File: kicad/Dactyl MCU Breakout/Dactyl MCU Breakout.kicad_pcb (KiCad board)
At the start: 4 copper layers, 99 x 61.1 mm, 74 parts, among them J202 Split, J203 Column, J204 Thumb, J205 External, J206 Row, J207 Display, J208 Vic, J209 JST, J302 Split, J303 Column, J304 Thumb, J305 External, J306 Row, J307 Display, J308 Vic, J309 JST, SW201 Battery, SW202 Reset, SW203 LED, SW301 Battery, SW302 Reset, SW303 LED, U201 SRV05-4, U202 Nice!Nano/2040, U301 SRV05-4, U302 Nice!Nano/2040

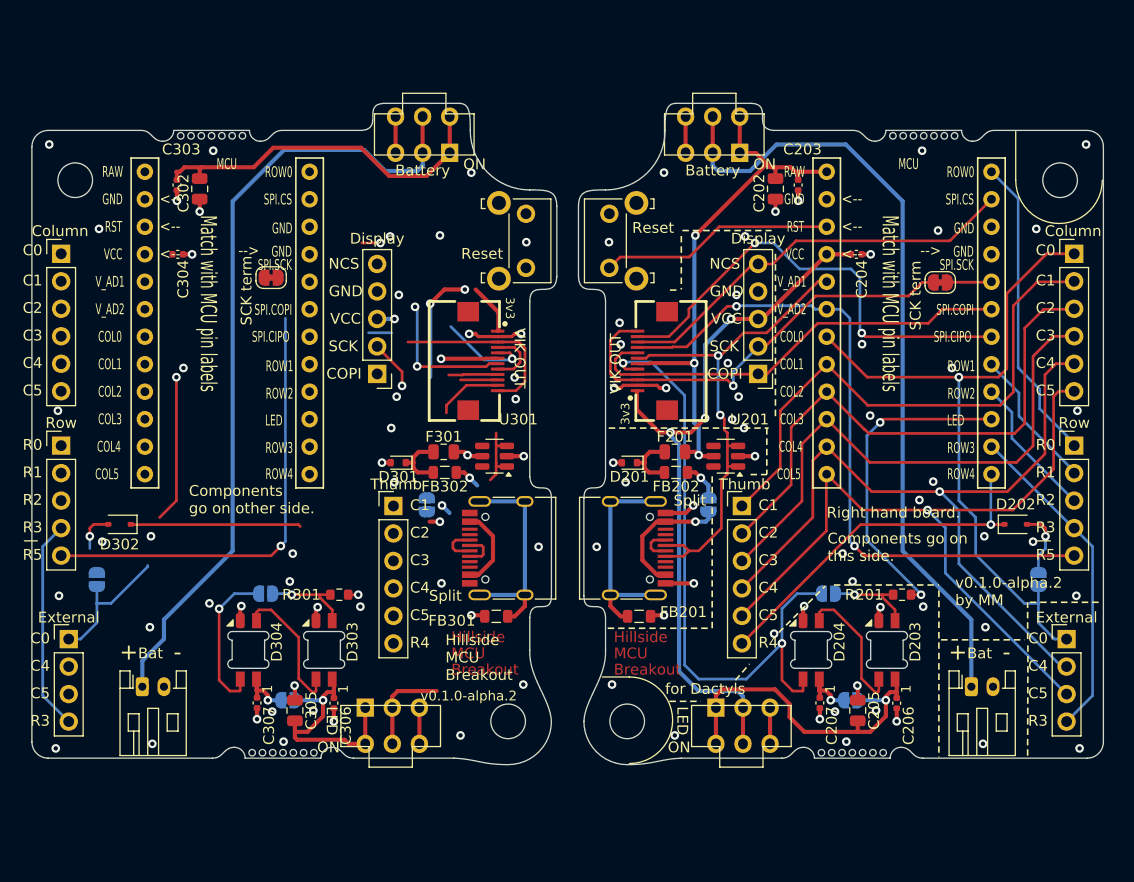
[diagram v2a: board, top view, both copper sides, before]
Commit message: feat(scheme): fix some mislabels
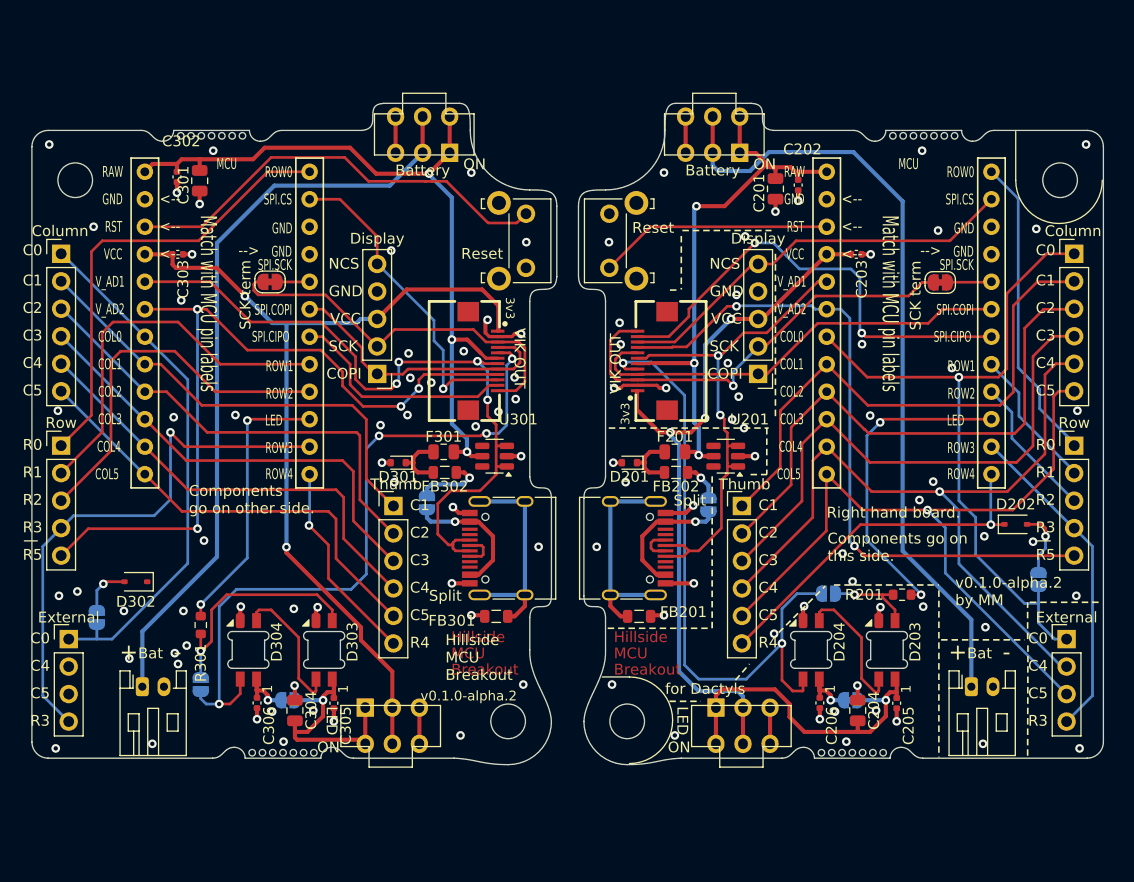
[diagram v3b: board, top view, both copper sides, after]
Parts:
- moved R301 13.1 mm to (65.6, 95.7), turned to -90 degrees
- moved JP304 10.3 mm to (65.6, 101.2), turned to -90 degrees
- moved D302 5.51 mm to (59.6, 91.7)
- moved JP302 3.50 mm to (56.0, 95.0)
- moved C301 0.75 mm to (65.5, 54.6)
- moved C302 0.75 mm to (63.4, 54.3)
- moved JP303 0.41 mm to (72.0, 64.0)
- moved JP301 0.20 mm to (86.5, 84.4)
- renumbered C202 to C201, C203 to C202, C204 to C203, C205 to C204, C206 to C205, C207 to C206, C302 to C301, C303 to C302, C304 to C303, C305 to C304, C306 to C305, C307 to C306, J209 to J201, J309 to J301
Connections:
- C301 pad 2: /Right/RAW -> /Left/RAW
- C302 pad 2: /Right/RAW -> /Left/RAW
- C303 pad 2: /Right/VCC -> /Left/VCC
- C304 pad 2: /Right/VCC_LED1 -> /Left/VCC_LED1
- C305 pad 2: /Right/VCC_LED1 -> /Left/VCC_LED1
- C306 pad 2: /Right/VCC_LED2 -> /Left/VCC_LED2
- D301 pad 1: /Right/RAW_BEADED -> /Left/RAW_BEADED
- D302 pad 1: /Right/row4 -> /Left/row4
- D302 pad 2: Net-(D202-A) -> Net-(D302-A)
- D303 pad 1: /Right/VCC_LED1 -> /Left/VCC_LED1
- D303 pad 2: Net-(D203-DOUT) -> Net-(D303-DOUT)
- D303 pad 4: Net-(D203-DIN) -> Net-(D303-DIN)
- D304 pad 1: /Right/VCC_LED2 -> /Left/VCC_LED2
- D304 pad 2: /Right/LED_out -> /Left/LED_out
- D304 pad 4: Net-(D203-DOUT) -> Net-(D303-DOUT)
- F301 pad 1: /Right/RAW_BEADED -> /Left/RAW_BEADED
- F301 pad 2: /Right/RAW -> /Left/RAW
- FB301 pad 1: /Right/SHIELD -> /Left/SHIELD
- FB302 pad 1: /Right/RAW_ENABLED -> /Left/RAW_ENABLED
- FB302 pad 2: /Right/RAW_BEADED -> /Left/RAW_BEADED
- J301 pad 1: /Right/bat+ -> /Left/bat+
- J302 pad A4: /Right/split_RAW -> /Left/split_RAW
- J302 pad A5: unconnected-(J202-CC1-PadA5) -> unconnected-(J302-CC1-PadA5)
- J302 pad A6: /Right/SPLIT_VIK_GP_AD1 -> /Left/SPLIT_VIK_GP_AD1
- J302 pad A7: Net-(J202-D--PadA7) -> Net-(J302-D--PadA7)
- J302 pad A8: unconnected-(J202-SBU1-PadA8) -> unconnected-(J302-SBU1-PadA8)
- J302 pad A9: /Right/split_RAW -> /Left/split_RAW
- J302 pad B4: /Right/split_RAW -> /Left/split_RAW
- J302 pad B5: unconnected-(J202-CC2-PadB5) -> unconnected-(J302-CC2-PadB5)
- J302 pad B6: /Right/SPLIT_VIK_GP_AD1 -> /Left/SPLIT_VIK_GP_AD1
- J302 pad B7: Net-(J202-D--PadA7) -> Net-(J302-D--PadA7)
- J302 pad B8: unconnected-(J202-SBU2-PadB8) -> unconnected-(J302-SBU2-PadB8)
- J302 pad B9: /Right/split_RAW -> /Left/split_RAW
- J302 pad S1: /Right/SHIELD -> /Left/SHIELD
- J303 pad 1: /Right/col0 -> /Left/col0
- J303 pad 2: /Right/col1 -> /Left/col1
- J303 pad 3: /Right/col2 -> /Left/col2
- J303 pad 4: /Right/col3 -> /Left/col3
- J303 pad 5: /Right/col4 -> /Left/col4
- J303 pad 6: /Right/col5 -> /Left/col5
- J304 pad 1: /Right/col1 -> /Left/col1
- J304 pad 2: /Right/col2 -> /Left/col2
- J304 pad 3: /Right/col3 -> /Left/col3
- J304 pad 4: /Right/col4 -> /Left/col4
- J304 pad 5: /Right/col5 -> /Left/col5
- J304 pad 6: /Right/row4 -> /Left/row4
- J305 pad 1: /Right/col0 -> /Left/col0
- J305 pad 2: /Right/col4 -> /Left/col4
- J305 pad 3: /Right/col5 -> /Left/col5
- J305 pad 4: /Right/row3 -> /Left/row3
- J306 pad 1: /Right/row0 -> /Left/row0
- J306 pad 2: /Right/row1 -> /Left/row1
- J306 pad 3: /Right/row2 -> /Left/row2
- J306 pad 4: /Right/row3 -> /Left/row3
- J306 pad 5: /Right/row5_VIK_GP_AD2 -> /Left/row5_VIK_GP_AD2
- J307 pad 1: /Right/SPI0.COPI/SCL -> /Left/SPI0.COPI/SCL
- J307 pad 2: /Right/SPI0.SCK/SDA -> /Left/SPI0.SCK/SDA
- J307 pad 3: /Right/VCC -> /Left/VCC
- J307 pad 5: /Right/SPI0.SC -> /Left/SPI0.SC
- J308 pad 1: /Right/VCC -> /Left/VCC
- J308 pad 10: /Right/SPI0.SC -> /Left/SPI0.SC
- J308 pad 11: /Right/SPI0.CIPO -> /Left/SPI0.CIPO
- J308 pad 12: /Right/SPI0.SCK/SDA -> /Left/SPI0.SCK/SDA
- J308 pad 3: /Right/SPI0.SCK/SDA -> /Left/SPI0.SCK/SDA
- J308 pad 4: /Right/SPI0.COPI/SCL -> /Left/SPI0.COPI/SCL
- J308 pad 5: /Right/LED_out -> /Left/LED_out
- J308 pad 6: /Right/RAW -> /Left/RAW
- J308 pad 7: /Right/SPLIT_VIK_GP_AD1 -> /Left/SPLIT_VIK_GP_AD1
- J308 pad 8: /Right/SPI0.COPI/SCL -> /Left/SPI0.COPI/SCL
- J308 pad 9: /Right/row5_VIK_GP_AD2 -> /Left/row5_VIK_GP_AD2
- JP301 pad 1: /Right/split_RAW -> /Left/split_RAW
- JP301 pad 2: /Right/RAW_ENABLED -> /Left/RAW_ENABLED
- JP302 pad 1: /Right/col0 -> /Left/col0
- JP302 pad 2: Net-(D202-A) -> Net-(D302-A)
- JP303 pad 1: Net-(JP203-A) -> Net-(JP303-A)
- JP303 pad 2: /Right/SPI0.SCK/SDA -> /Left/SPI0.SCK/SDA
- JP304 pad 1: Net-(D203-DIN) -> Net-(D303-DIN)
- JP304 pad 2: /Right/LED_out -> /Left/LED_out
- JP305 pad 1: /Right/VCC_LED1 -> /Left/VCC_LED1
- JP305 pad 2: /Right/VCC_LED2 -> /Left/VCC_LED2
- R301 pad 1: /Right/LED -> /Left/LED
- R301 pad 2: Net-(D203-DIN) -> Net-(D303-DIN)
- SW301 pad 1: /Right/RAW -> /Left/RAW
- SW301 pad 2: /Right/bat+ -> /Left/bat+
- SW301 pad 3: unconnected-(SW201-C-Pad3)_0 -> unconnected-(SW301-C-Pad3)_0
- SW302 pad 2: /Right/RST -> /Left/RST
- SW303 pad 1: /Right/VCC_LED1 -> /Left/VCC_LED1
- SW303 pad 2: /Right/VCC -> /Left/VCC
- SW303 pad 3: unconnected-(SW203-C-Pad3)_0 -> unconnected-(SW303-C-Pad3)_1
- U301 pad 1: /Right/SPLIT_VIK_GP_AD1 -> /Left/SPLIT_VIK_GP_AD1
- U301 pad 3: /Right/SPLIT_VIK_GP_AD1 -> /Left/SPLIT_VIK_GP_AD1
- U301 pad 4: unconnected-(U201-IO3-Pad4) -> unconnected-(U301-IO3-Pad4)
- U301 pad 5: /Right/RAW -> /Left/RAW
- U301 pad 6: unconnected-(U201-IO4-Pad6) -> unconnected-(U301-IO4-Pad6)
- U302 pad 1: /Right/row0 -> /Left/row0
- U302 pad 10: /Right/LED -> /Left/LED
- U302 pad 11: /Right/row3 -> /Left/row3
- U302 pad 12: /Right/row4 -> /Left/row4
- U302 pad 13: /Right/col5 -> /Left/col5
- U302 pad 14: /Right/col4 -> /Left/col4
- U302 pad 15: /Right/col3 -> /Left/col3
- U302 pad 16: /Right/col2 -> /Left/col2
- U302 pad 17: /Right/col1 -> /Left/col1
- U302 pad 18: /Right/col0 -> /Left/col0
- U302 pad 19: /Right/row5_VIK_GP_AD2 -> /Left/row5_VIK_GP_AD2
- U302 pad 2: /Right/SPI0.SC -> /Left/SPI0.SC
- U302 pad 20: /Right/SPLIT_VIK_GP_AD1 -> /Left/SPLIT_VIK_GP_AD1
- U302 pad 21: /Right/VCC -> /Left/VCC
- U302 pad 22: /Right/RST -> /Left/RST
- U302 pad 24: /Right/RAW -> /Left/RAW
- U302 pad 5: Net-(JP203-A) -> Net-(JP303-A)
- U302 pad 6: /Right/SPI0.COPI/SCL -> /Left/SPI0.COPI/SCL
- U302 pad 7: /Right/SPI0.CIPO -> /Left/SPI0.CIPO
- U302 pad 8: /Right/row1 -> /Left/row1
- U302 pad 9: /Right/row2 -> /Left/row2
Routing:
- net /Left/VCC: track 0.00 -> 79.7 mm, vias 0 -> 2
- net /Left/row5_VIK_GP_AD2: track 0.00 -> 72.7 mm, vias 0 -> 4
- net /Right/bat+: track 139.6 -> 69.0 mm
- net /Left/SPLIT_VIK_GP_AD1: track 0.00 -> 68.2 mm, vias 0 -> 4
- net /Left/RAW: track 0.00 -> 67.5 mm, vias 0 -> 3
- net /Left/bat+: track 0.00 -> 66.3 mm
- net /Left/LED_out: track 0.00 -> 63.8 mm, vias 0 -> 4
- net /Left/row3: track 0.00 -> 50.4 mm, vias 0 -> 1
- net /Left/col0: track 0.00 -> 48.7 mm
- net /Right/row5_VIK_GP_AD2: track 110.1 -> 63.6 mm, vias 3 -> 2
- net /Left/col2: track 0.00 -> 42.8 mm
- net /Left/col1: track 0.00 -> 42.5 mm
- net /Left/row0: track 0.00 -> 42.3 mm
- net /Left/col3: track 0.00 -> 42.0 mm
- net /Left/col4: track 0.00 -> 41.6 mm
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
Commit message: feat(pcb): finish routing left board
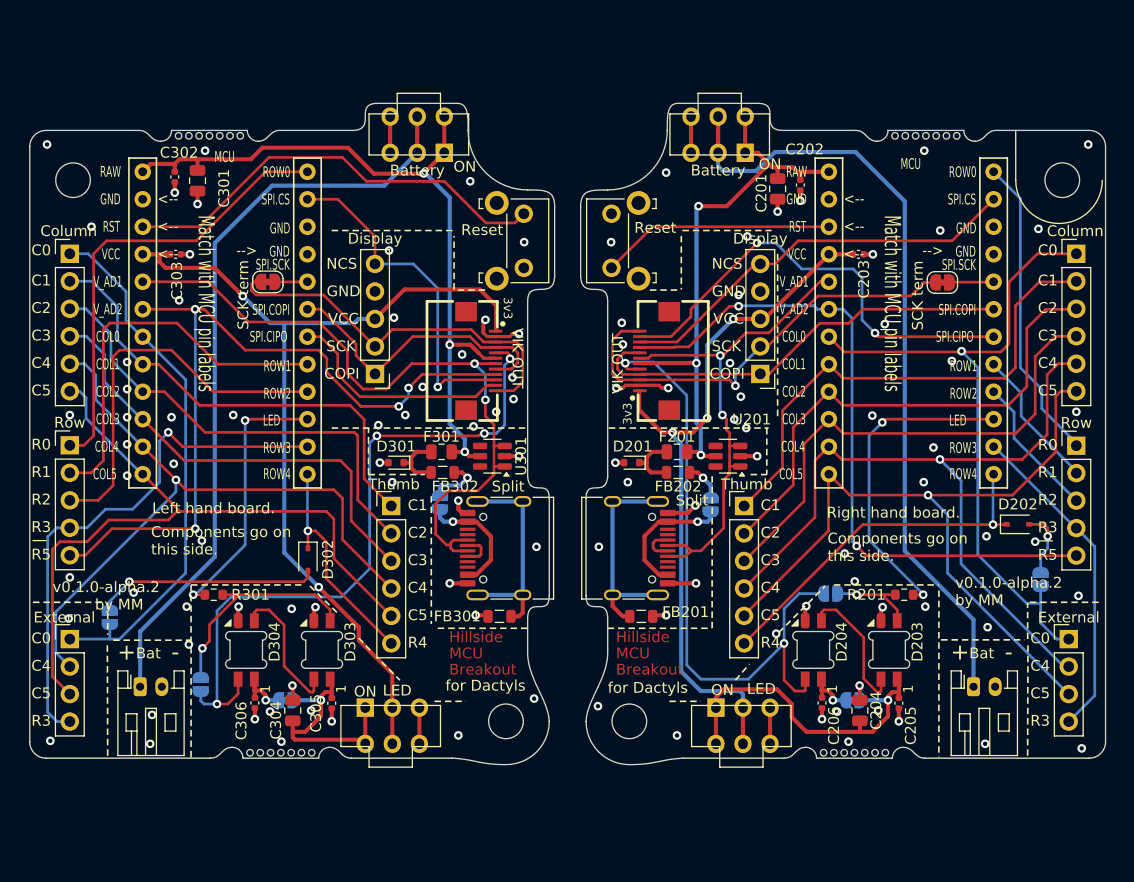
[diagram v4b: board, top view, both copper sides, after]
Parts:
- moved D302 16.0 mm to (75.5, 89.7), turned to -90 degrees
- moved R301 3.05 mm to (66.8, 92.9), turned to 0 degrees
- moved JP301 1.20 mm to (87.7, 84.4)
- moved JP302 1.20 mm to (57.2, 95.0)
- moved J306 0.80 mm to (53.5, 79.1)
- moved J303 0.80 mm to (53.5, 61.4)
- moved SW201 0.50 mm to (113.4, 50.4)
- moved SW301 0.50 mm to (85.6, 50.4)
- moved FB301 0.30 mm to (93.2, 94.9)
- moved J205 0.20 mm to (145.8, 97.0)
- moved C201 0.20 mm to (118.9, 55.4)
- moved C202 0.20 mm to (121.0, 55.0)
- moved C203 0.20 mm to (126.4, 61.5)
- moved C204 0.20 mm to (126.5, 103.6)
- moved C206 0.20 mm to (123.0, 102.9)
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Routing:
- net /Left/col5: track 41.5 -> 68.8 mm
- net /Left/col4: track 41.6 -> 64.3 mm, vias 0 -> 1
- net Net-(D302-A): track 4.73 -> 20.7 mm
- net /Right/col2: track 50.8 -> 46.6 mm
- net /Right/col3: track 50.6 -> 46.6 mm
- net /Right/col1: track 50.2 -> 46.8 mm
- net /Left/SPI0.SC: track 30.2 -> 32.2 mm
- net /Left/row4: track 18.9 -> 20.9 mm
- net /Left/SPI0.COPI/SCL: track 26.4 -> 27.9 mm
- net /Left/split_RAW: track 12.5 -> 11.1 mm
- net /Left/SPLIT_VIK_GP_AD1: track 68.2 -> 66.8 mm, vias 4 -> 2
- net /Left/RAW_ENABLED: track 6.45 -> 5.17 mm
- net /Left/row2: track 35.1 -> 36.3 mm
- net Net-(D303-DIN): track 21.6 -> 20.5 mm
- net /Left/row5_VIK_GP_AD2: track 72.7 -> 71.7 mm
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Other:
- board size 99 x 61.1 mm -> 99.4 x 61.1 mm
- board text added: "Left hand board."

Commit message: feat: make GND local to board half
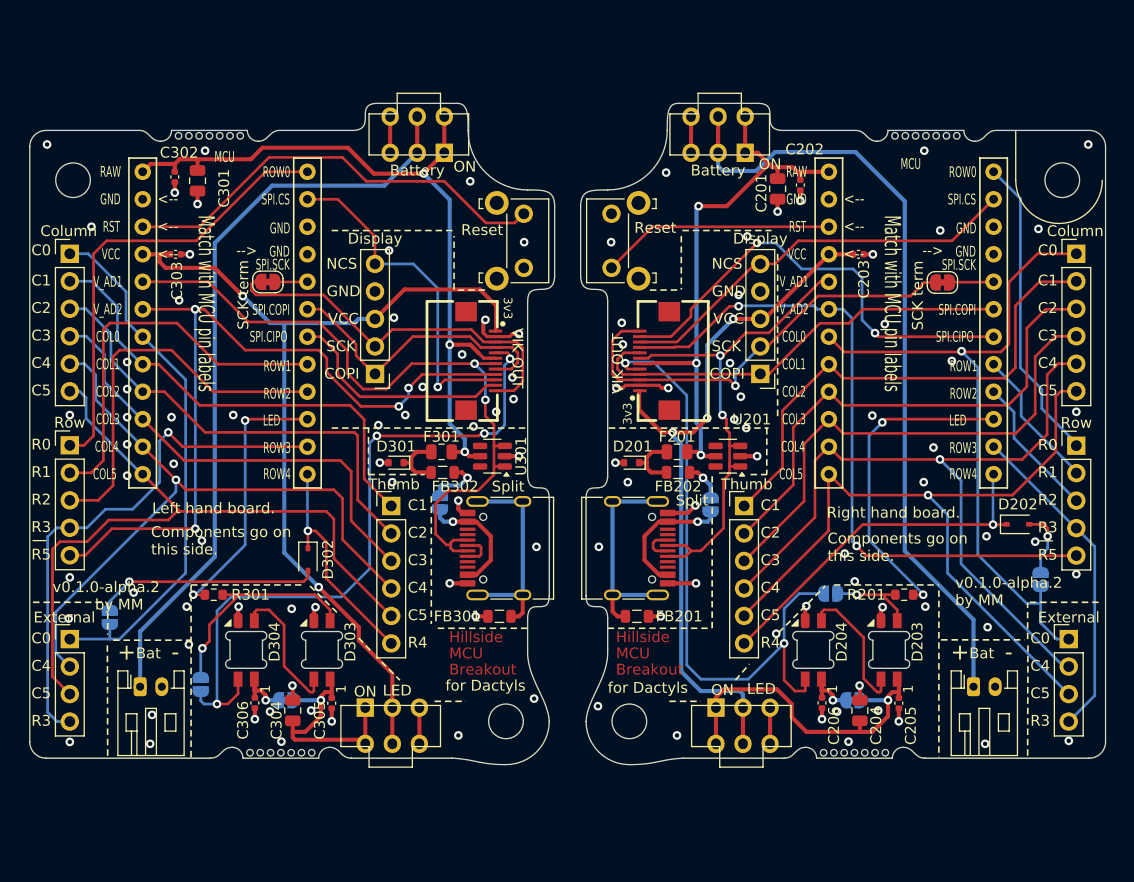
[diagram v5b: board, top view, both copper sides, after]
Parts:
- moved FB201 0.40 mm to (105.9, 94.9)
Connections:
- C201 pad 1: GND -> /Right/GND
- C202 pad 1: GND -> /Right/GND
- C203 pad 1: GND -> /Right/GND
- C204 pad 1: GND -> /Right/GND
- C205 pad 1: GND -> /Right/GND
- C206 pad 1: GND -> /Right/GND
- C301 pad 1: GND -> /Left/GND
- C302 pad 1: GND -> /Left/GND
- C303 pad 1: GND -> /Left/GND
- C304 pad 1: GND -> /Left/GND
- C305 pad 1: GND -> /Left/GND
- C306 pad 1: GND -> /Left/GND
- D201 pad 2: GND -> /Right/GND
- D203 pad 3: GND -> /Right/GND
- D204 pad 3: GND -> /Right/GND
- D301 pad 2: GND -> /Left/GND
- D303 pad 3: GND -> /Left/GND
- D304 pad 3: GND -> /Left/GND
- FB201 pad 2: GND -> /Right/GND
- FB301 pad 2: GND -> /Left/GND
- J201 pad 2: GND -> /Right/GND
- J202 pad A1: GND -> /Right/GND
- J202 pad A12: GND -> /Right/GND
- J202 pad B1: GND -> /Right/GND
- J202 pad B12: GND -> /Right/GND
- J207 pad 4: GND -> /Right/GND
- J208 pad 2: GND -> /Right/GND
- J301 pad 2: GND -> /Left/GND
- J302 pad A1: GND -> /Left/GND
- J302 pad A12: GND -> /Left/GND
- J302 pad B1: GND -> /Left/GND
- J302 pad B12: GND -> /Left/GND
- J307 pad 4: GND -> /Left/GND
- J308 pad 2: GND -> /Left/GND
- SW202 pad 1: GND -> /Right/GND
- SW302 pad 1: GND -> /Left/GND
- U201 pad 2: GND -> /Right/GND
- U202 pad 23: GND -> /Right/GND
- U202 pad 3: GND -> /Right/GND
- U202 pad 4: GND -> /Right/GND
- U301 pad 2: GND -> /Left/GND
- U302 pad 23: GND -> /Left/GND
- U302 pad 3: GND -> /Left/GND
- U302 pad 4: GND -> /Left/GND
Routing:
- net GND: track 43.0 -> 0.00 mm, vias 109 -> 0
- net /Right/GND: track 0.00 -> 23.3 mm, vias 0 -> 52
- net /Left/GND: track 0.00 -> 20.2 mm, vias 0 -> 57
- added copper zone on In1.Cu, net /Left/GND
- added copper zone on In2.Cu, net /Left/GND
- added copper zone on In1.Cu, net /Right/GND
- added copper zone on In2.Cu, net /Right/GND
- removed copper zone on In1.Cu, net GND
- removed copper zone on In2.Cu, net GND
